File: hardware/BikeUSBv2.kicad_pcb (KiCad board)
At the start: 2 copper layers, 43.6 x 25.5 mm, 57 parts, among them J1 TYPE-C-31-M-16, J2 JST S2B-EH(LF)(SN), Q1 2SB772SQ, SW1 1TS002E-2500-2501-CT, SW2 1TS002E-2500-2501-CT, U1 TPS63070, U2 ATtiny1616-M, U3 FUSB302B10MPX, U4 HT7550, U5 TL431AIDBZR

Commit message: fix AC RDIV
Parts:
- R4: value 10k -> 27k
- R8: value 10k -> 3k
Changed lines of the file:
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@@
     (descr "Resistor SMD 0805 (2012 Metric), square (rectangular) end terminal, IPC_7351 nominal with elongated pad for handsoldering. (Body size source: IPC-SM-782 page 72, https://www.pcb-3d.com/wordpress/wp-content/uploads/ipc-sm-782a_amendment_1_and_2.pdf), generated with kicad-footprint-generator")
     (tags "resistor handsolder")
-    (property "LCSC" "C217770")
+    (property "LCSC" "C375523")
     (property "Sheetfile" "BikeUSBv2.kicad_sch")
     (property "Sheetname" "")
@@
         (effects (font (size 1 1) (thickness 0.15)))
     )
-    (fp_text value "10k" (at 0 1.65) (layer "F.Fab")
+    (fp_text value "27k" (at 0 1.65) (layer "F.Fab")
         (effects (font (size 1 1) (thickness 0.15)))
     )
@@
     (descr "Resistor SMD 0805 (2012 Metric), square (rectangular) end terminal, IPC_7351 nominal with elongated pad for handsoldering. (Body size source: IPC-SM-782 page 72, https://www.pcb-3d.com/wordpress/wp-content/uploads/ipc-sm-782a_amendment_1_and_2.pdf), generated with kicad-footprint-generator")
     (tags "resistor handsolder")
-    (property "LCSC" "C217770")
+    (property "LCSC" "C218519")
     (property "Sheetfile" "BikeUSBv2.kicad_sch")
     (property "Sheetname" "")
@@
         (effects (font (size 1 1) (thickness 0.15)))
     )
-    (fp_text value "10k" (at 0 1.65) (layer "F.Fab")
-        (effects (font (size 1 1) (thickness 0.15)))
-    )
+    (fp_text value "3k" (at 0 1.65) (layer "F.Fab")
+        (effects (font (size 1 1) (thickness 0.15)))
+    )

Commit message: [PCB] fix resistors
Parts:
- R6: value 680k -> 130k
- R7: value 130k -> 24k
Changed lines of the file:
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@@
         (effects (font (size 1 1) (thickness 0.15)))
     )
-    (fp_text value "680k" (at 0 1.65 90) (layer "F.Fab")
+    (fp_text value "130k" (at 0 1.65 90) (layer "F.Fab")
         (effects (font (size 1 1) (thickness 0.15)))
     )
@@
     (descr "Resistor SMD 0805 (2012 Metric), square (rectangular) end terminal, IPC_7351 nominal with elongated pad for handsoldering. (Body size source: IPC-SM-782 page 72, https://www.pcb-3d.com/wordpress/wp-content/uploads/ipc-sm-782a_amendment_1_and_2.pdf), generated with kicad-footprint-generator")
     (tags "resistor handsolder")
-    (property "LCSC" "C2831651")
     (property "Sheetfile" "BikeUSBv2.kicad_sch")
     (property "Sheetname" "")
@@
         (effects (font (size 1 1) (thickness 0.15)))
     )
-    (fp_text value "130k" (at 0 1.65 90) (layer "F.Fab")
-        (effects (font (size 1 1) (thickness 0.15)))
-    )
+    (fp_text value "24k" (at 0 1.65 90) (layer "F.Fab")
+        (effects (font (size 1 1) (thickness 0.15)))
+    )

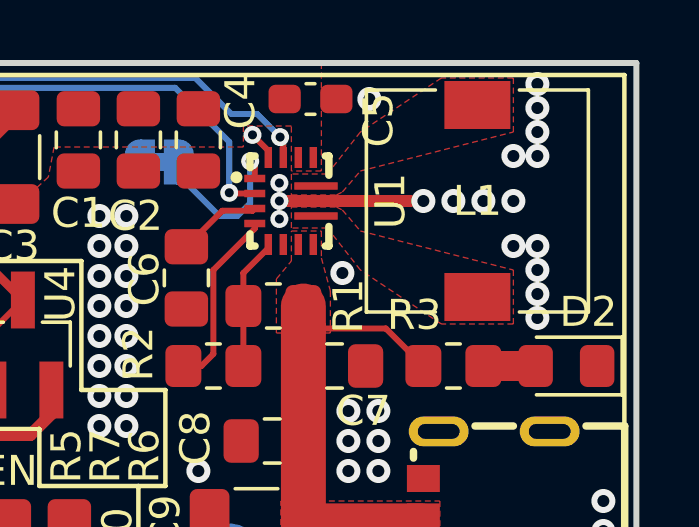
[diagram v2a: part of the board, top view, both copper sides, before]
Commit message: [PCB] move L1 back to leave more room for U1 heatsink
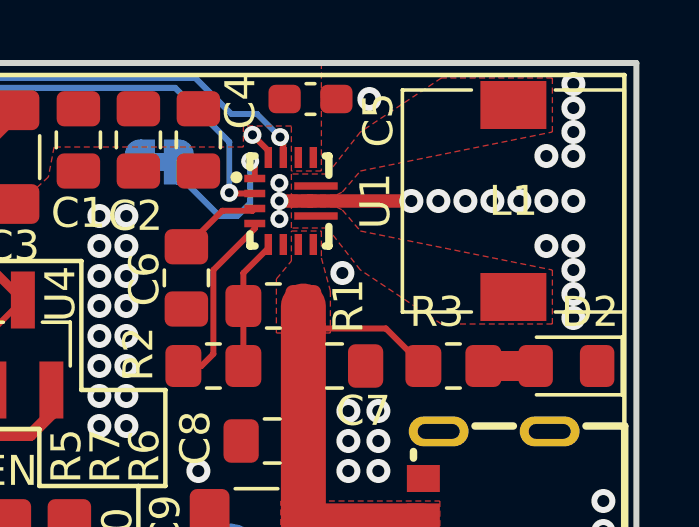
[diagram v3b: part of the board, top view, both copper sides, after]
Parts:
- moved REF** 2.28 mm to (148.1, 90.7)
- moved L1 1.20 mm to (149.5, 87.0)
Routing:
- net GND: track 23.3 -> 23.0 mm, vias 96 -> 99
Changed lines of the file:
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@@
     (property "ki_keywords" "LED diode")
     (attr smd)
-    (fp_text reference "D2" (at -0.7325 1.8 180) (layer "F.SilkS")
+    (fp_text reference "D2" (at -0.7825 1.8 180) (layer "F.SilkS")
         (effects (font (size 1 1) (thickness 0.15)))
     )
@@
   )
   (footprint "Inductor_SMD:L_7.3x7.3_H4.5" (layer "F.Cu")
-    (at 148.3 87 -90)
+    (at 149.5 87 -90)
     (descr "Choke, SMD, 7.3x7.3mm 4.5mm height")
     (tags "Choke SMD")
@@
     (descr "Resistor SMD 0805 (2012 Metric), square (rectangular) end terminal, IPC_7351 nominal with elongated pad for handsoldering. (Body size source: IPC-SM-782 page 72, https://www.pcb-3d.com/wordpress/wp-content/uploads/ipc-sm-782a_amendment_1_and_2.pdf), generated with kicad-footprint-generator")
     (tags "resistor handsolder")
-    (property "LCSC" "C218663")
+    (property "LCSC" "C2831651")
     (property "Sheetfile" "BikeUSBv2.kicad_sch")
     (property "Sheetname" "")
@@
     (property "ki_keywords" "Buck-Boost adjustable converter")
     (attr smd)
-    (fp_text reference "U1" (at 0 -3.5 90) (layer "F.SilkS")
+    (fp_text reference "U1" (at 0 -3 90) (layer "F.SilkS")
         (effects (font (size 1 1) (thickness 0.15)))
     )
@@
     (descr "Resistor SMD 0805 (2012 Metric), square (rectangular) end terminal, IPC_7351 nominal with elongated pad for handsoldering. (Body size source: IPC-SM-782 page 72, https://www.pcb-3d.com/wordpress/wp-content/uploads/ipc-sm-782a_amendment_1_and_2.pdf), generated with kicad-footprint-generator")
     (tags "resistor handsolder")
+    (property "LCSC" "C218452")
     (property "Sheetfile" "BikeUSBv2.kicad_sch")
     (property "Sheetname" "")
@@
     (property "ki_keywords" "R res resistor")
     (attr smd)
-    (fp_text reference "R3" (at 1.3 1.7 180) (layer "F.SilkS")
+    (fp_text reference "R3" (at 0.55 1.8 180) (layer "F.SilkS")
         (effects (font (size 1 1) (thickness 0.15)))
     )
@@
   )
   (footprint "Symbol:OSHW-Logo_5.7x6mm_SilkScreen" (layer "B.Cu")
-    (at 150.3 90.1 180)
+    (at 148.1 90.7 180)
     (descr "Open Source Hardware Logo")
     (tags "Logo OSHW")
@@
   (segment (start 140.803647 84.796353) (end 141.33 85.322706) (width 0.2) (layer "F.Cu") (net 1))
   (segment (start 139.5 92.1) (end 139.1 92.5) (width 0.2) (layer "F.Cu") (net 1))
-  (segment (start 142.72 87) (end 146.5 87) (width 0.4) (layer "F.Cu") (net 1))
   (segment (start 141.33 85.322706) (end 141.33 85.55) (width 0.2) (layer "F.Cu") (net 1))
   (segment (start 140.88 87.92) (end 139.5 89.3) (width 0.2) (layer "F.Cu") (net 1))
@@
   (segment (start 140.88 87.75) (end 140.88 87.92) (width 0.2) (layer "F.Cu") (net 1))
   (segment (start 120.5 94.65) (end 113 94.65) (width 2) (layer "F.Cu") (net 1))
+  (segment (start 142.72 87) (end 146.2 87) (width 0.45) (layer "F.Cu") (net 1))
   (segment (start 139.5 89.3) (end 139.5 92.1) (width 0.2) (layer "F.Cu") (net 1))
-  (segment (start 142.72 87) (end 141.7 87) (width 0.4) (layer "F.Cu") (net 1))
+  (segment (start 142.72 87) (end 141.7 87) (width 0.45) (layer "F.Cu") (net 1))
   (segment (start 126.375 102.175) (end 127.825 102.175) (width 0.2) (layer "F.Cu") (net 1))
   (segment (start 146.5 101.75) (end 147.5 101.75) (width 0.9) (layer "F.Cu") (net 1))
-  (via (at 150.3 83.1) (size 0.8) (drill 0.4) (layers "F.Cu" "B.Cu") (free) (net 1))
+  (via (at 151.5 83.1) (size 0.8) (drill 0.4) (layers "F.Cu" "B.Cu") (free) (net 1))
   (via (at 116.35 94.3) (size 0.8) (drill 0.4) (layers "F.Cu" "B.Cu") (free) (net 1))
   (via (at 147.75 100.75) (size 0.8) (drill 0.4) (layers "F.Cu" "B.Cu") (free) (net 1))
@@
   (via (at 126.2 95.8) (size 0.8) (drill 0.4) (layers "F.Cu" "B.Cu") (free) (net 1))
   (via (at 123.6 88.7) (size 0.8) (drill 0.4) (layers "F.Cu" "B.Cu") (net 1))
-  (via (at 150.3 84.7) (size 0.8) (drill 0.4) (layers "F.Cu" "B.Cu") (free) (net 1))
+  (via (at 151.5 84.7) (size 0.8) (drill 0.4) (layers "F.Cu" "B.Cu") (free) (net 1))
   (via (at 135.7 92.5) (size 0.8) (drill 0.4) (layers "F.Cu" "B.Cu") (free) (net 1))
   (via (at 152.5 99) (size 0.8) (drill 0.4) (layers "F.Cu" "B.Cu") (free) (net 1))
@@
   (via (at 141 99) (size 0.8) (drill 0.4) (layers "F.Cu" "B.Cu") (free) (net 1))
   (via (at 117.05 94.3) (size 0.8) (drill 0.4) (layers "F.Cu" "B.Cu") (free) (net 1))
-  (via (at 147.5 87) (size 0.8) (drill 0.4) (layers "F.Cu" "B.Cu") (free) (net 1))
+  (via (at 147.9 87) (size 0.8) (drill 0.4) (layers "F.Cu" "B.Cu") (free) (net 1))
   (via (at 136.6 91.5) (size 0.8) (drill 0.4) (layers "F.Cu" "B.Cu") (free) (net 1))
   (via (at 144 102) (size 0.8) (drill 0.4) (layers "F.Cu" "B.Cu") (free) (net 1))
@@
   (via (at 141.7 87) (size 0.6) (drill 0.3) (layers "F.Cu" "B.Cu") (free) (net 1))
   (via (at 135.7 90.5) (size 0.8) (drill 0.4) (layers "F.Cu" "B.Cu") (free) (net 1))
+  (via (at 151.5 87) (size 0.8) (drill 0.4) (layers "F.Cu" "B.Cu") (free) (net 1))
   (via (at 122.8 88.7) (size 0.8) (drill 0.4) (layers "F.Cu" "B.Cu") (net 1))
   (via (at 136.6 92.5) (size 0.8) (drill 0.4) (layers "F.Cu" "B.Cu") (free) (net 1))
@@
   (via (at 116.75 103) (size 0.8) (drill 0.4) (layers "F.Cu" "B.Cu") (free) (net 1))
   (via (at 135.7 93.5) (size 0.8) (drill 0.4) (layers "F.Cu" "B.Cu") (free) (net 1))
-  (via (at 150.3 90.9) (size 0.8) (drill 0.4) (layers "F.Cu" "B.Cu") (free) (net 1))
-  (via (at 150.3 90.1) (size 0.8) (drill 0.4) (layers "F.Cu" "B.Cu") (free) (net 1))
+  (via (at 151.5 90.9) (size 0.8) (drill 0.4) (layers "F.Cu" "B.Cu") (free) (net 1))
+  (via (at 151.5 90.1) (size 0.8) (drill 0.4) (layers "F.Cu" "B.Cu") (free) (net 1))
   (via (at 136.6 87.5) (size 0.8) (drill 0.4) (layers "F.Cu" "B.Cu") (free) (net 1))
   (via (at 123.6 87.9) (size 0.8) (drill 0.4) (layers "F.Cu" "B.Cu") (net 1))
@@
   (via (at 135.7 88.5) (size 0.8) (drill 0.4) (layers "F.Cu" "B.Cu") (free) (net 1))
   (via (at 136.6 88.5) (size 0.8) (drill 0.4) (layers "F.Cu" "B.Cu") (free) (net 1))
-  (via (at 146.5 87) (size 0.8) (drill 0.4) (layers "F.Cu" "B.Cu") (free) (net 1))
-  (via (at 150.3 83.9) (size 0.8) (drill 0.4) (layers "F.Cu" "B.Cu") (free) (net 1))
+  (via (at 146.1 87) (size 0.8) (drill 0.4) (layers "F.Cu" "B.Cu") (free) (net 1))
+  (via (at 151.5 83.9) (size 0.8) (drill 0.4) (layers "F.Cu" "B.Cu") (free) (net 1))
   (via (at 114.6 95) (size 0.8) (drill 0.4) (layers "F.Cu" "B.Cu") (free) (net 1))
-  (via (at 149.5 85.5) (size 0.8) (drill 0.4) (layers "F.Cu" "B.Cu") (free) (net 1))
-  (via (at 150.3 88.5) (size 0.8) (drill 0.4) (layers "F.Cu" "B.Cu") (free) (net 1))
-  (via (at 148.5 87) (size 0.8) (drill 0.4) (layers "F.Cu" "B.Cu") (free) (net 1))
+  (via (at 150.6 85.5) (size 0.8) (drill 0.4) (layers "F.Cu" "B.Cu") (free) (net 1))
+  (via (at 151.5 88.5) (size 0.8) (drill 0.4) (layers "F.Cu" "B.Cu") (free) (net 1))
+  (via (at 148.8 87) (size 0.8) (drill 0.4) (layers "F.Cu" "B.Cu") (free) (net 1))
   (via (at 118.8 95) (size 0.8) (drill 0.4) (layers "F.Cu" "B.Cu") (free) (net 1))
   (via (at 143.8 89.4) (size 0.8) (drill 0.4) (layers "F.Cu" "B.Cu") (free) (net 1))
@@
   (via (at 114.25 102) (size 0.8) (drill 0.4) (layers "F.Cu" "B.Cu") (free) (net 1))
   (via (at 116.75 102) (size 0.8) (drill 0.4) (layers "F.Cu" "B.Cu") (free) (net 1))
-  (via (at 149.5 88.5) (size 0.8) (drill 0.4) (layers "F.Cu" "B.Cu") (free) (net 1))
+  (via (at 150.6 88.5) (size 0.8) (drill 0.4) (layers "F.Cu" "B.Cu") (free) (net 1))
   (via (at 137.5 103.75) (size 0.8) (drill 0.4) (layers "F.Cu" "B.Cu") (net 1))
   (via (at 140.803647 84.796353) (size 0.6) (drill 0.3) (layers "F.Cu" "B.Cu") (free) (net 1))
-  (via (at 150.3 89.3) (size 0.8) (drill 0.4) (layers "F.Cu" "B.Cu") (free) (net 1))
+  (via (at 151.5 89.3) (size 0.8) (drill 0.4) (layers "F.Cu" "B.Cu") (free) (net 1))
   (via (at 114.25 103) (size 0.8) (drill 0.4) (layers "F.Cu" "B.Cu") (free) (net 1))
   (via (at 117.75 94.3) (size 0.8) (drill 0.4) (layers "F.Cu" "B.Cu") (free) (net 1))
-  (via (at 150.3 85.5) (size 0.8) (drill 0.4) (layers "F.Cu" "B.Cu") (free) (net 1))
+  (via (at 151.5 85.5) (size 0.8) (drill 0.4) (layers "F.Cu" "B.Cu") (free) (net 1))
   (via (at 147.75 101.5) (size 0.8) (drill 0.4) (layers "F.Cu" "B.Cu") (free) (net 1))
   (via (at 130.1 103.8) (size 0.8) (drill 0.4) (layers "F.Cu" "B.Cu") (free) (net 1))
@@
   (via (at 135.7 91.5) (size 0.8) (drill 0.4) (layers "F.Cu" "B.Cu") (free) (net 1))
   (via (at 130.1 106) (size 0.8) (drill 0.4) (layers "F.Cu" "B.Cu") (free) (net 1))
+  (via (at 147 87) (size 0.8) (drill 0.4) (layers "F.Cu" "B.Cu") (free) (net 1))
   (via (at 145 103) (size 0.8) (drill 0.4) (layers "F.Cu" "B.Cu") (free) (net 1))
   (via (at 152.5 97) (size 0.8) (drill 0.4) (layers "F.Cu" "B.Cu") (free) (net 1))
@@
   (via (at 147.75 102.25) (size 0.8) (drill 0.4) (layers "F.Cu" "B.Cu") (free) (net 1))
   (via (at 145 94) (size 0.8) (drill 0.4) (layers "F.Cu" "B.Cu") (free) (net 1))
-  (via (at 149.5 87) (size 0.8) (drill 0.4) (layers "F.Cu" "B.Cu") (free) (net 1))
+  (via (at 149.7 87) (size 0.8) (drill 0.4) (layers "F.Cu" "B.Cu") (free) (net 1))
   (via (at 145 95) (size 0.8) (drill 0.4) (layers "F.Cu" "B.Cu") (free) (net 1))
   (via (at 130.1 107) (size 0.8) (drill 0.4) (layers "F.Cu" "B.Cu") (free) (net 1))
@@
   (via (at 135.7 89.5) (size 0.8) (drill 0.4) (layers "F.Cu" "B.Cu") (free) (net 1))
   (via (at 116 102.5) (size 0.8) (drill 0.4) (layers "F.Cu" "B.Cu") (free) (net 1))
+  (via (at 150.6 87) (size 0.8) (drill 0.4) (layers "F.Cu" "B.Cu") (free) (net 1))
   (via (at 117.4 95) (size 0.8) (drill 0.4) (layers "F.Cu" "B.Cu") (free) (net 1))
   (via (at 152.5 101) (size 0.8) (drill 0.4) (layers "F.Cu" "B.Cu") (free) (net 1))
@@
         (xy 143.8 87.3)
         (xy 144.4 88)
-        (xy 149.5 89.3)
-        (xy 149.5 91.1)
+        (xy 150.8 89.3)
+        (xy 150.8 91.1)
         (xy 147.1 91.1)
         (xy 144.4 89.3)
@@
         (xy 143.8 86.7)
         (xy 144.4 86)
-        (xy 149.5 84.7)
-        (xy 149.5 82.9)
+        (xy 150.8 84.7)
+        (xy 150.8 82.9)
         (xy 147.1 82.9)
         (xy 144.4 84.7)

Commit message: [PCB] add kicad logo and gpl text
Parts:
- added REF**: KiCad-Logo2_5mm_SilkScreen, Symbol:KiCad-Logo2_5mm_SilkScreen, B.Cu at (143.8, 90.4)
- moved REF** 23.9 mm to (124.3, 92.9)
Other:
- board text added: "GNU GPL 3.0"

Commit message: [PCB] move OSHW logo away from via
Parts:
- moved REF** 1.14 mm to (123.2, 93.2)
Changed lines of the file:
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@@
   )
   (footprint "Symbol:OSHW-Logo_5.7x6mm_SilkScreen" (layer "B.Cu")
-    (at 124.3 92.9 180)
+    (at 123.2 93.2 180)
     (descr "Open Source Hardware Logo")
     (tags "Logo OSHW")

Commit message: [PCB] add CC testpads
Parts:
- added TP7: CC1, TestPoint:TestPoint_Pad_D1.5mm, B.Cu at (142.7, 104.9)
- added TP8: CC2, TestPoint:TestPoint_Pad_D1.5mm, B.Cu at (139.0, 104.9)
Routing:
- net /CC1: track 20.4 -> 21.5 mm, vias 0 -> 1
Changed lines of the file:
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@@
       (net 3 "+5V") (pinfunction "1") (pintype "passive"))
   )
+  (footprint "TestPoint:TestPoint_Pad_D1.5mm" (layer "B.Cu")
+    (at 139.000707 104.876793 90)
+    (descr "SMD pad as test Point, diameter 1.5mm")
+    (tags "test point SMD pad")
+    (property "Sheetfile" "BikeUSBv2.kicad_sch")
+    (property "Sheetname" "")
+    (property "exclude_from_bom" "")
+    (property "ki_description" "test point")
+    (property "ki_keywords" "test point tp")
+    (attr exclude_from_pos_files exclude_from_bom)
+    (fp_text reference "TP8" (at -1.823207 -2.300707 90) (layer "B.Fab")
+        (effects (font (size 1 1) (thickness 0.15)) (justify mirror))
+    )
+    (fp_text value "CC2" (at -1.823207 0.099293 180) (layer "B.SilkS")
+        (effects (font (size 1 1) (thickness 0.15)) (justify mirror))
+    )
+    (fp_text user "${REFERENCE}" (at 0 1.65 90) (layer "B.Fab")
+        (effects (font (size 1 1) (thickness 0.15)) (justify mirror))
+    )
+    (fp_circle (center 0 0) (end 0 -0.95)
+      (stroke (width 0.12) (type solid)) (fill none) (layer "B.SilkS"))
+    (fp_circle (center 0 0) (end 1.25 0)
+      (stroke (width 0.05) (type solid)) (fill none) (layer "B.CrtYd"))
+    (pad "1" smd circle (at 0 0 90) (size 1.5 1.5) (layers "B.Cu" "B.Mask")
+      (net 25 "/CC2") (pinfunction "1") (pintype "passive"))
+  )
+  (footprint "TestPoint:TestPoint_Pad_D1.5mm" (layer "B.Cu")
+    (at 142.7 104.9 90)
+    (descr "SMD pad as test Point, diameter 1.5mm")
+    (tags "test point SMD pad")
+    (property "Sheetfile" "BikeUSBv2.kicad_sch")
+    (property "Sheetname" "")
+    (property "exclude_from_bom" "")
+    (property "ki_description" "test point")
+    (property "ki_keywords" "test point tp")
+    (attr exclude_from_pos_files exclude_from_bom)
+    (fp_text reference "TP7" (at 0 1.648 90) (layer "B.Fab")
+        (effects (font (size 1 1) (thickness 0.15)) (justify mirror))
+    )
+    (fp_text value "CC1" (at -1.8 0 180) (layer "B.SilkS")
+        (effects (font (size 1 1) (thickness 0.15)) (justify mirror))
+    )
+    (fp_text user "${REFERENCE}" (at 0 1.65 90) (layer "B.Fab")
+        (effects (font (size 1 1) (thickness 0.15)) (justify mirror))
+    )
+    (fp_circle (center 0 0) (end 0 -0.95)
+      (stroke (width 0.12) (type solid)) (fill none) (layer "B.SilkS"))
+    (fp_circle (center 0 0) (end 1.25 0)
+      (stroke (width 0.05) (type solid)) (fill none) (layer "B.CrtYd"))
+    (pad "1" smd circle (at 0 0 90) (size 1.5 1.5) (layers "B.Cu" "B.Mask")
+      (net 27 "/CC1") (pinfunction "1") (pintype "passive"))
+  )
   (footprint "Symbol:OSHW-Logo_5.7x6mm_SilkScreen" (layer "B.Cu")
     (at 123.2 93.2 180)
@@
     (property "ki_keywords" "cap capacitor")
     (attr through_hole)
-    (fp_text reference "C14" (at 7.602651 0) (layer "B.SilkS")
+    (fp_text reference "C14" (at 2.302651 -5 -90) (layer "B.SilkS")
         (effects (font (size 1 1) (thickness 0.15)) (justify mirror))
     )
@@
       ))
   )
-  (gr_rect (start 133.4 95.2) (end 136.8 100.4)
+  (gr_rect (start 145.1 86.4) (end 150.3 83)
     (stroke (width 0.15) (type default)) (fill none) (layer "B.SilkS"))
   (gr_line (start 137 101.8) (end 137 96.5)
@@
     (effects (font (size 1 1) (thickness 0.15)) (justify bottom mirror))
   )
-  (gr_text "GNU\nGPL\n3.0" (at 135.1 97.9) (layer "B.SilkS")
+  (gr_text "GNU\nGPL\n3.0" (at 147.8 84.7 90) (layer "B.SilkS")
     (effects (font (size 1 1) (thickness 0.15)) (justify mirror))
   )
-  (gr_text "@h3wastooshort\n/BikeUSBv2" (at 153 107) (layer "B.SilkS")
+  (gr_text "@h3wastooshort\n/BikeUSBv2" (at 134.5 91.7 90) (layer "B.SilkS")
     (effects (font (size 1 1) (thickness 0.2) bold) (justify left bottom mirror))
   )
@@
   (segment (start 145.25 104.75) (end 148 104.75) (width 0.2) (layer "F.Cu") (net 27))
   (segment (start 148.6 100.6) (end 147.5 99.5) (width 0.2) (layer "F.Cu") (net 27))
-  (segment (start 137.488854 106) (end 144 106) (width 0.2) (layer "F.Cu") (net 27))
   (segment (start 136.2375 104.7375) (end 136.5125 105.0125) (width 0.2) (layer "F.Cu") (net 27))
+  (segment (start 142.7 106) (end 142.7 104.9) (width 0.2) (layer "F.Cu") (net 27))
   (segment (start 136.75 105.0125) (end 136.75 105.261146) (width 0.2) (layer "F.Cu") (net 27))
   (segment (start 144 106) (end 145.25 104.75) (width 0.2) (layer "F.Cu") (net 27))
   (segment (start 136.5125 105.0125) (end 136.75 105.0125) (width 0.2) (layer "F.Cu") (net 27))
   (segment (start 136.75 105.261146) (end 137.488854 106) (width 0.2) (layer "F.Cu") (net 27))
+  (segment (start 142.1 106) (end 144 106) (width 0.2) (layer "F.Cu") (net 27))
   (segment (start 136.2375 104.25) (end 136.2375 104.7375) (width 0.2) (layer "F.Cu") (net 27))
   (segment (start 148.6 104.15) (end 148.6 100.6) (width 0.2) (layer "F.Cu") (net 27))
+  (segment (start 137.488854 106) (end 142.1 106) (width 0.2) (layer "F.Cu") (net 27))
   (segment (start 147.5 99.5) (end 146.5 99.5) (width 0.2) (layer "F.Cu") (net 27))
+  (via (at 142.7 104.9) (size 0.8) (drill 0.4) (layers "F.Cu" "B.Cu") (net 27))
   (segment (start 135.754 101.854) (end 137.033 101.854) (width 0.2) (layer "F.Cu") (net 28))
   (segment (start 135.155378 101.155378) (end 135.155378 101.255378) (width 0.2) (layer "F.Cu") (net 28))

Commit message: [PCB] move text and such
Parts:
- moved REF** 0.14 mm to (123.3, 93.3)
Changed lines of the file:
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@@
   )
   (footprint "Symbol:OSHW-Logo_5.7x6mm_SilkScreen" (layer "B.Cu")
-    (at 123.2 93.2 180)
+    (at 123.3 93.3 180)
     (descr "Open Source Hardware Logo")
     (tags "Logo OSHW")
@@
       ))
   )
-  (gr_rect (start 145.1 86.4) (end 150.3 83)
+  (gr_rect (start 126.7 91.5) (end 130.1 96.7)
     (stroke (width 0.15) (type default)) (fill none) (layer "B.SilkS"))
   (gr_line (start 137 101.8) (end 137 96.5)
@@
     (effects (font (size 1 1) (thickness 0.15)) (justify bottom mirror))
   )
-  (gr_text "GNU\nGPL\n3.0" (at 147.8 84.7 90) (layer "B.SilkS")
+  (gr_text "GNU\nGPL\n3.0" (at 128.4 94.2) (layer "B.SilkS")
     (effects (font (size 1 1) (thickness 0.15)) (justify mirror))
   )
-  (gr_text "@h3wastooshort\n/BikeUSBv2" (at 134.5 91.7 90) (layer "B.SilkS")
+  (gr_text "@h3wastooshort\n/BikeUSBv2" (at 134.5 91.5 90) (layer "B.SilkS")
     (effects (font (size 1 1) (thickness 0.2) bold) (justify left bottom mirror))
   )

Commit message: [PCB] add I2C testpads and improve groundplane
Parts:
- added TP10: SCL, TestPoint:TestPoint_Pad_D1.5mm, B.Cu at (136.4, 105.2)
- added TP9: SDA, TestPoint:TestPoint_Pad_D1.5mm, B.Cu at (133.8, 105.2)
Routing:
- net /PG: track 52.3 -> 68.3 mm
- net /EN: track 52.4 -> 68.3 mm
- net /CC2: track 26.4 -> 20.7 mm
- net /SCL: track 14.7 -> 16.7 mm, vias 2 -> 3
- net /SDA: track 9.17 -> 10.3 mm, vias 0 -> 1
- net /AC2: track 15.9 -> 16.5 mm
- net GND: vias 99 -> 102
